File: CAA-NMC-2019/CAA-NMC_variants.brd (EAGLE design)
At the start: 100.2 x 100.4 mm, 28 parts, among them IC1 ATTINY85-20SU, J1 M20-9980346

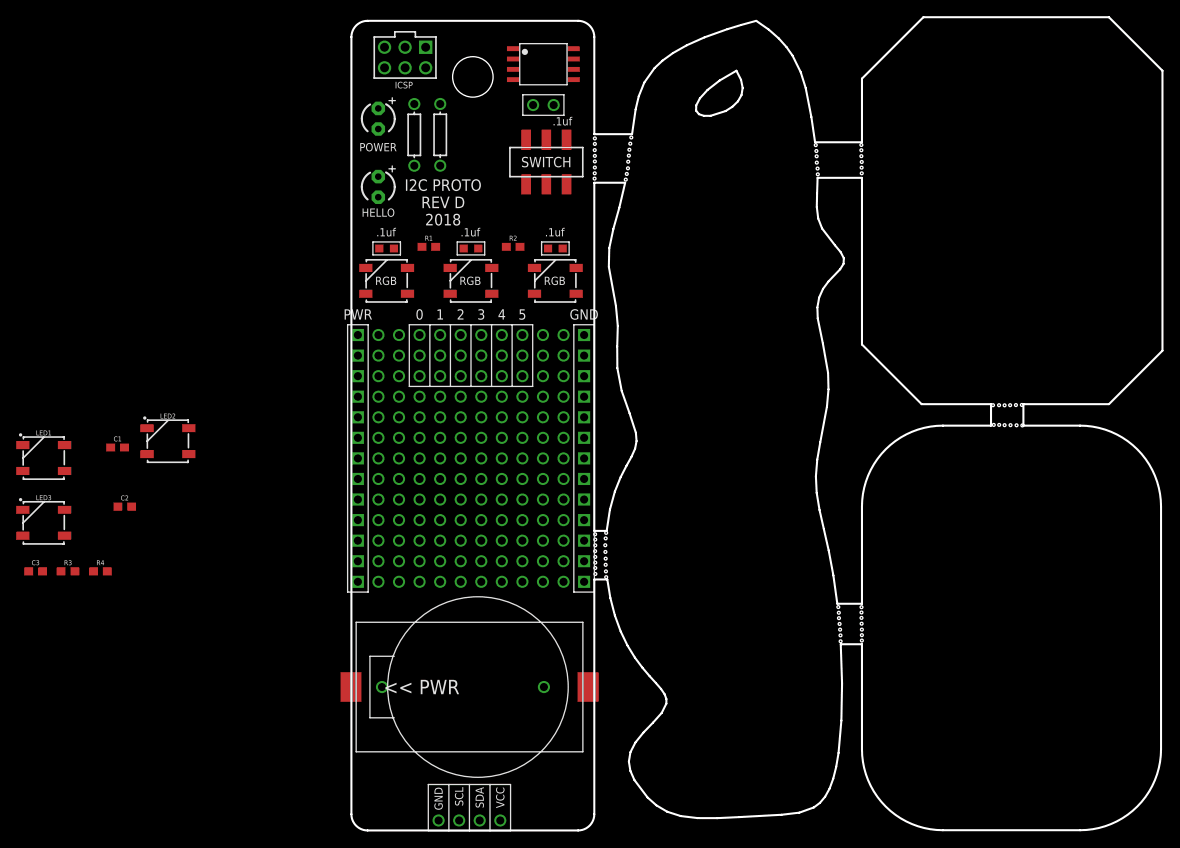
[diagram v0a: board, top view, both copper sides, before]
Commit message: added organic layout
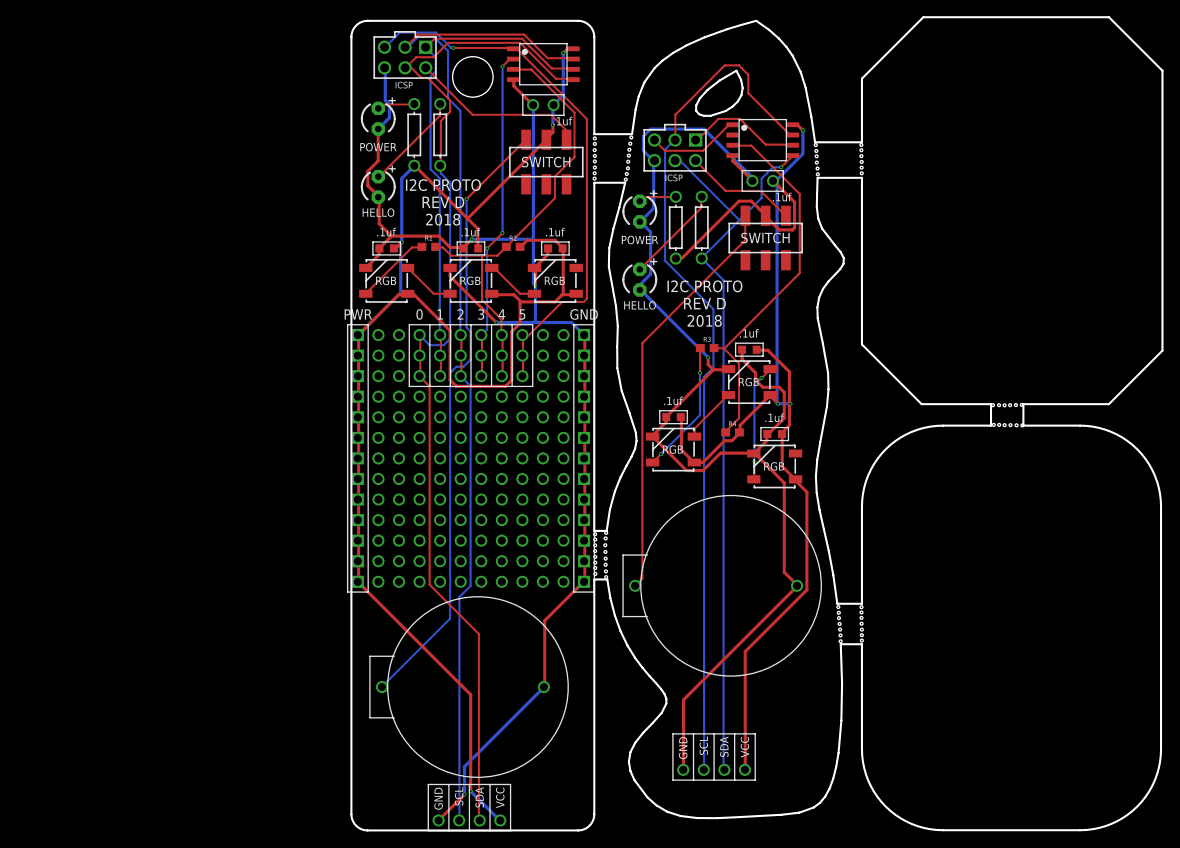
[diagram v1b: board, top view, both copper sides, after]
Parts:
- removed C1, C2, C3: 0.1uF, SparkFun-Capacitors:0603
- removed LED1, LED2, LED3: WS2812B, SparkFun-LED:WS2812B
- removed U$2: SMT-BATTERY-HOLDER, BadgeParts:SMT-CR-HOLDER
- added D4, D5, D6: WS2812B, BadgeParts:WS2812B
- added HELLO1, POWER1: LED3MM, BadgeParts:LED3MM
- added IC2: ATTINY85-20SU, BadgeParts:SOT127P798X216-8N
- added J2: M20-9980346, BadgeParts:HDRV6W64P254_2X3_762X508X868P
- added U$10, U$9: RESISTOR, BadgeParts:AXIAL-0.3
- added U$11: SMT-SWITCH, BadgeParts:SMT-SWITCH
- added U$14: THRU-CR-HOLDER, BadgeParts:THRU-CR-HOLDER
- added U$4: GND, BadgeParts:1X01
- added U$5: VCC, BadgeParts:1X01
- added U$6: SDA, BadgeParts:1X01
- added U$7: SCL, BadgeParts:1X01
- added U$8: DECOUPLING_CAP, BadgeParts:DECOUPLING_CAP
- moved R3 83.6 mm to (43.9, 59.6)
- moved R4 79.9 mm to (47.1, 49.2)
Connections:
- removed net N$12: LED1.4, R3.1
- removed net RGBLEDS: R3.2, R4.1
- removed net VDD: C1.1, C2.1, C3.1, LED1.1, LED2.1, LED3.1, R4.2
- new net GND1: D4.CAP1, D4.GND, D5.CAP1, D5.GND, D6.CAP1, D6.GND, HELLO1.NEG, IC2.GND, J2.GND, POWER1.NEG, U$14.GND, U$4.P$1, U$8.P$1
- new net N$6: POWER1.POS, U$9.P$3
- new net N$7: HELLO1.POS, U$10.P$3
- new net N$8: D4.DO, D5.DI
- new net PB10: IC2.PB5, J2.5/RST
- new net PB11: IC2.PB1, J2.1/MISO
- new net PB6: IC2.PB0, J2.0/MOSI/SDA, U$10.P$4, U$6.P$1
- new net PB7: IC2.PB3
- new net PB8: IC2.PB4, R3.2, R4.1
- new net PB9: IC2.PB2, J2.2/SCK/SCL, U$7.P$1
- new net VBAT1: U$11.4, U$14.VBAT
- new net VCC1: D4.CAP2, D4.VCC, D5.CAP2, D5.VCC, D6.CAP2, D6.VCC, IC2.VCC, R4.2, U$11.5, U$5.P$1, U$8.P$2, U$9.P$4
- new net VUSB1: J2.VCC, U$11.6
- net GND: no longer C1.2, C2.2, C3.2, LED1.3, LED2.3, LED3.3, U$2.GND
- net N$10: now also D4.DI, R3.1; no longer LED2.2, LED3.4
- net N$9: now also D5.DO, D6.DI; no longer LED1.2, LED2.4
- net VBAT: no longer U$2.VBAT
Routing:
- net VCC: track 0.00 -> 196.4 mm, vias 0 -> 4
- net GND: track 0.00 -> 172.6 mm, vias 0 -> 4
- net GND1: track 0.00 -> 149.4 mm, vias 0 -> 1
- net VCC1: track 0.00 -> 145.5 mm, vias 0 -> 3
- net PB0: track 0.00 -> 129.8 mm
- net PB2: track 0.00 -> 126.3 mm
- net PB9: track 0.00 -> 106.4 mm
- net PB6: track 0.00 -> 93.4 mm, vias 0 -> 1
- net VBAT: track 0.00 -> 75.9 mm, vias 0 -> 1
- net PB5: track 0.00 -> 67.6 mm, vias 0 -> 1
- net PB1: track 0.00 -> 62.4 mm
- net PB4: track 0.00 -> 55.6 mm
- net VBAT1: track 0.00 -> 51.3 mm
- net PB8: track 0.00 -> 46.8 mm
- net PB3: track 0.00 -> 41.2 mm, vias 0 -> 3
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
